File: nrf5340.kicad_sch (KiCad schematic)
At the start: 6 parts, among them U1 NRF5340

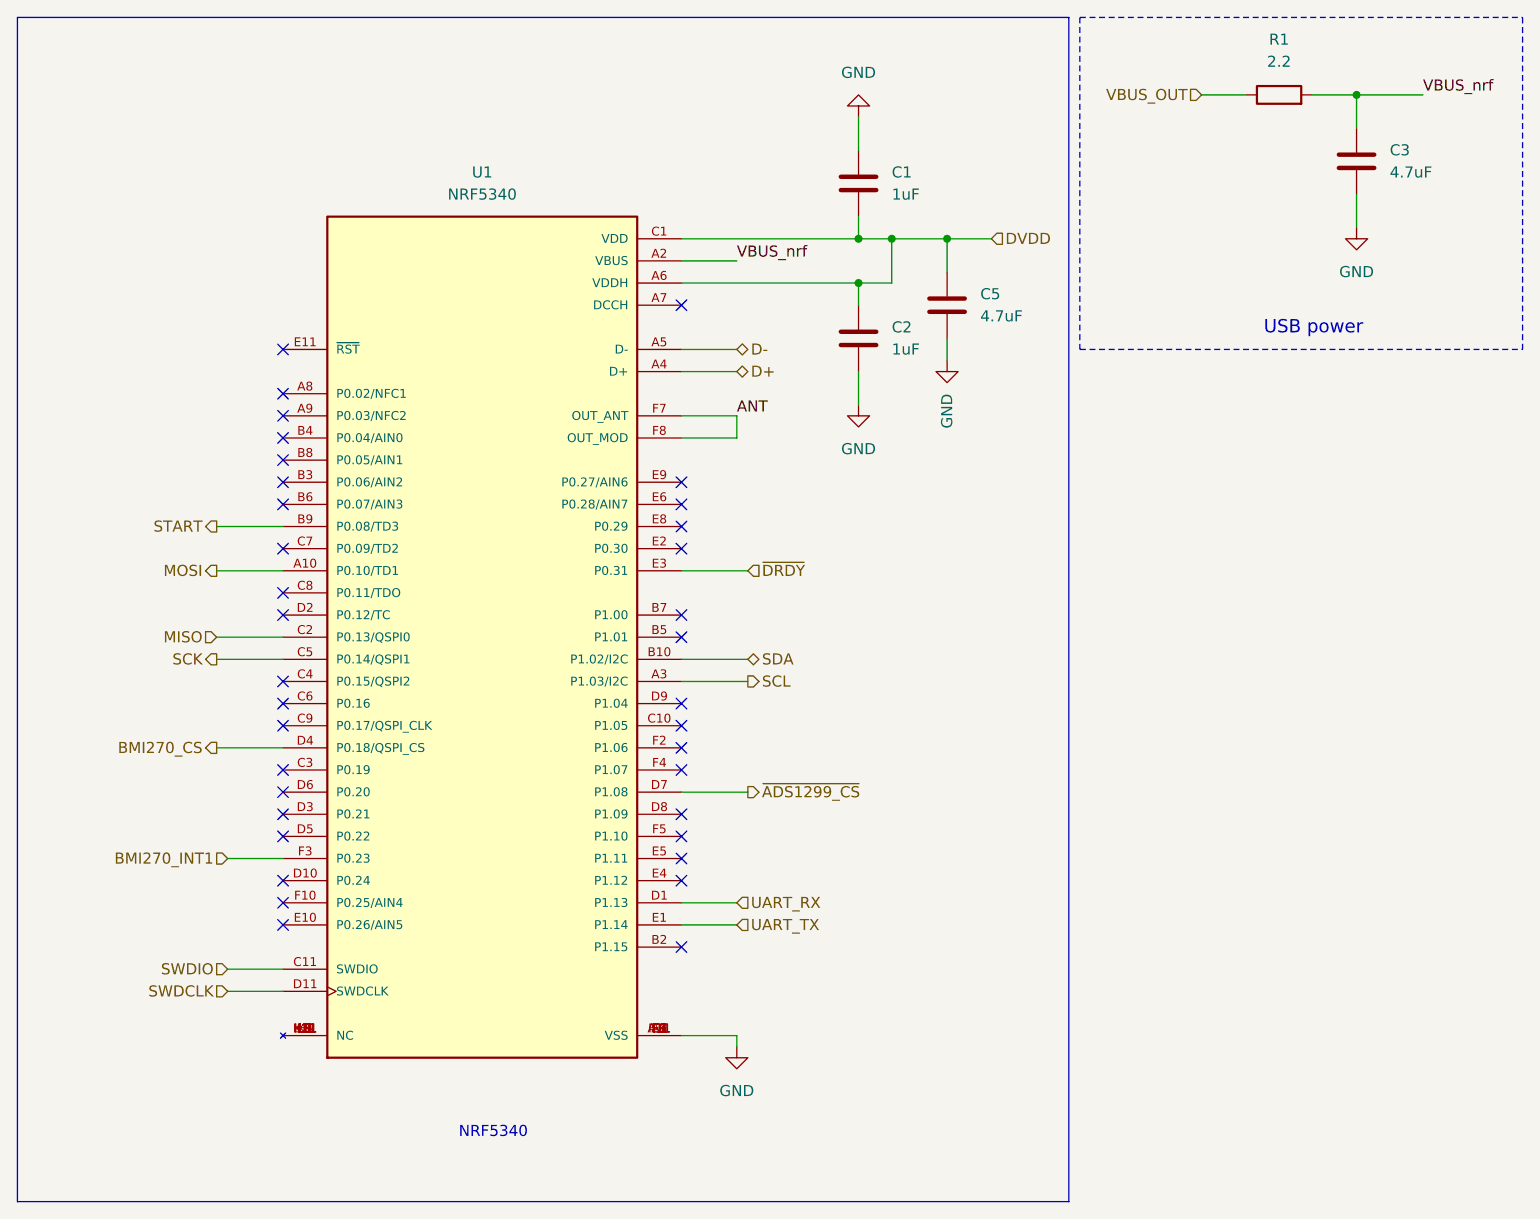
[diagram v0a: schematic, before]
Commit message: Feat: 개발보드 버전으로 PCB 변경
수정사항

단가 감소
- PCB Board size up (50x50)
- blind via 제거 (전체 레이아웃 수정)
- AVDD 전력평면 추가
- ADS1299 안쓰는핀 GND
- ADS1299 배치 변경 (Layout Reference 적용)

개발보드만 적용사항
- Pin Header size up 1.27 → 2.54mm
- PCB Size 50x50(mm)
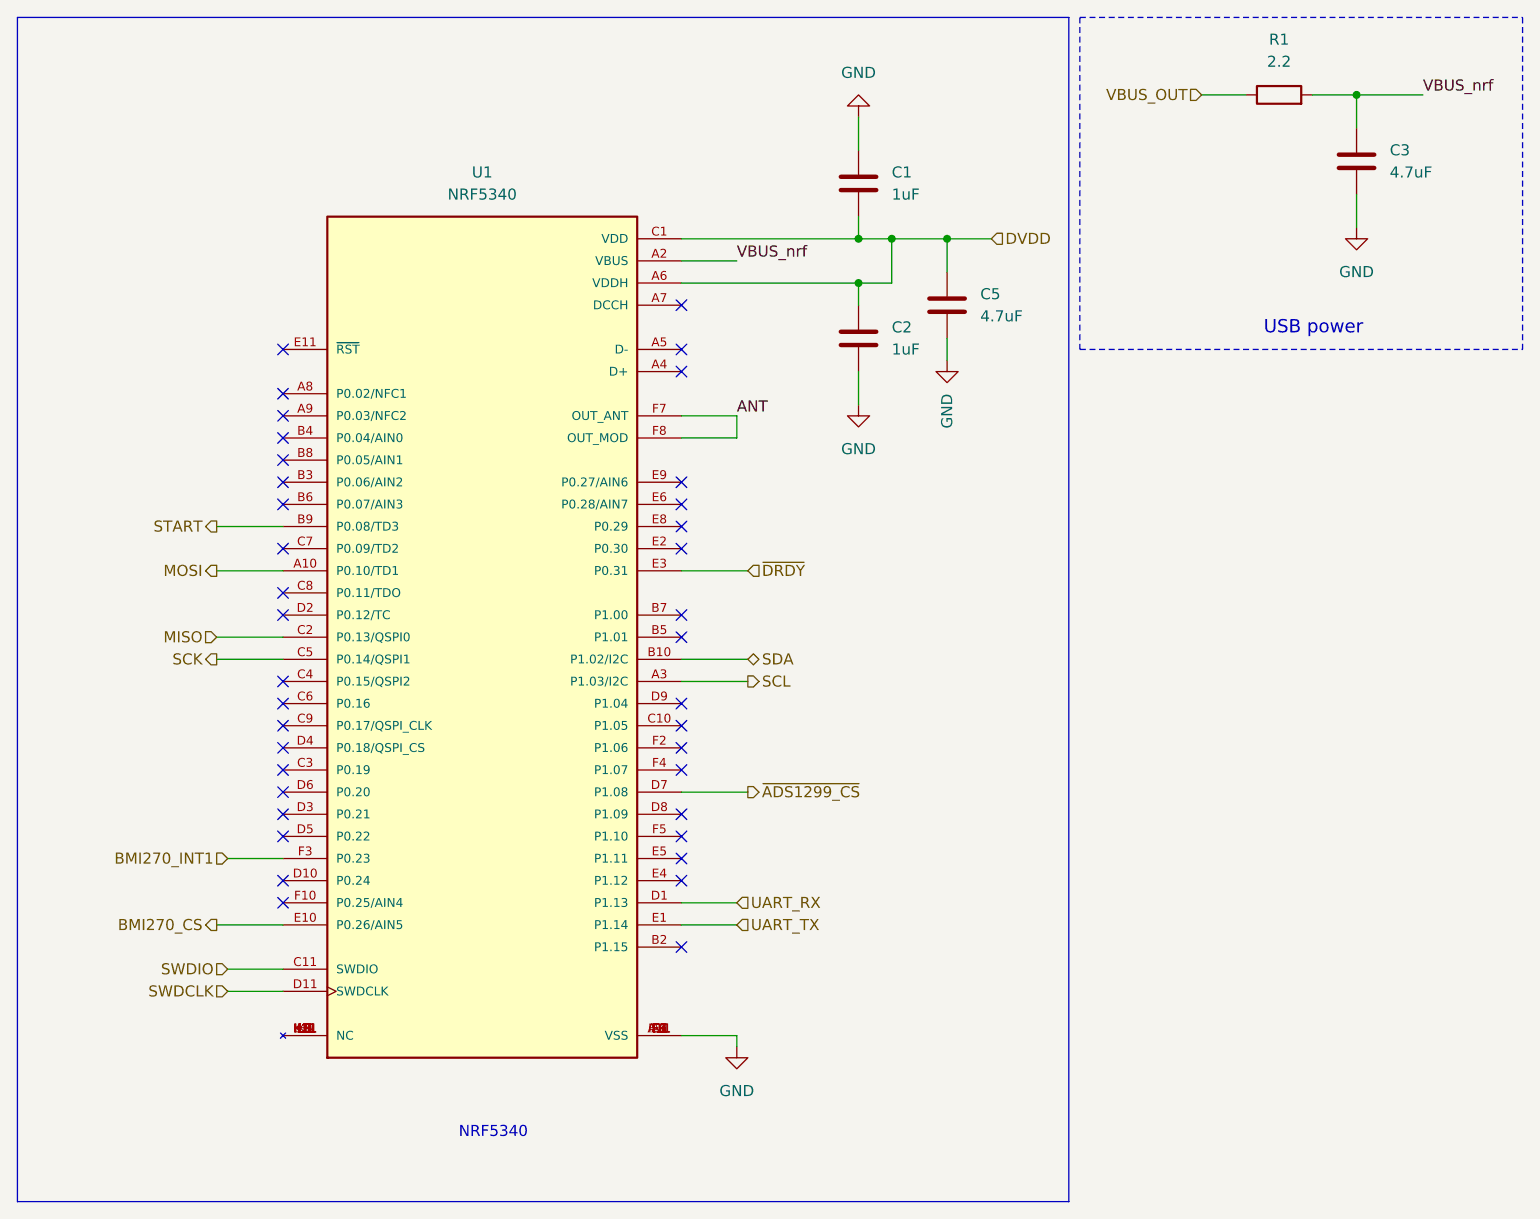
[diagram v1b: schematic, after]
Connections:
- net BMI270_CS: now also U1.E10 (P0.26/AIN5); no longer U1.D4 (P0.18/QSPI_CS)
- net D+: no longer names the net of U1.A4 (D+)
- net D-: no longer names the net of U1.A5 (D-)
- no-connect marks 36 -> 38
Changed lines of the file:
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@@
+	)
+	(no_connect
+		(at 43.18 66.04)
+	)
+	(no_connect
+		(at 43.18 73.66)
+	)
+	(no_connect
+		(at 88.9 66.04)
+	)
+	(no_connect
+		(at 43.18 55.88)
+	)
+	(no_connect
+		(at 88.9 45.72)
+	)
+	(no_connect
+		(at 88.9 83.82)
+	)
+	(no_connect
+		(at 88.9 81.28)
+	)
+	(no_connect
+		(at 88.9 68.58)
+	)
+	(no_connect
+		(at 88.9 111.76)
+	)
+	(no_connect
+		(at 43.18 104.14)
+	)
+	(no_connect
+		(at 88.9 53.34)
+	)
+	(no_connect
+		(at 43.18 91.44)
+	)
+	(no_connect
+		(at 88.9 119.38)
+	)
+	(no_connect
+		(at 43.18 78.74)
+	)
+	(no_connect
+		(at 43.18 68.58)
+	)
+	(no_connect
+		(at 88.9 109.22)
+	)
+	(no_connect
+		(at 43.18 93.98)
+	)
+	(no_connect
+		(at 43.18 63.5)
+	)
+	(no_connect
+		(at 88.9 91.44)
+	)
+	(no_connect
+		(at 88.9 73.66)
+	)
+	(no_connect
+		(at 88.9 104.14)
+	)
+	(no_connect
+		(at 88.9 99.06)
+	)
+	(no_connect
+		(at 88.9 50.8)
+	)
+	(no_connect
+		(at 43.18 99.06)
+	)
+	(no_connect
+		(at 43.18 111.76)
+	)
+	(no_connect
+		(at 43.18 101.6)
+	)
+	(no_connect
+		(at 43.18 60.96)
+	)
+	(no_connect
+		(at 43.18 58.42)
+	)
+	(no_connect
+		(at 88.9 96.52)
 	)
 	(no_connect
@@
 	)
 	(no_connect
-		(at 43.18 66.04)
-	)
-	(no_connect
-		(at 43.18 73.66)
-	)
-	(no_connect
-		(at 88.9 66.04)
-	)
-	(no_connect
-		(at 43.18 55.88)
-	)
-	(no_connect
-		(at 88.9 45.72)
-	)
-	(no_connect
-		(at 88.9 83.82)
-	)
-	(no_connect
-		(at 88.9 81.28)
-	)
-	(no_connect
-		(at 88.9 68.58)
-	)
-	(no_connect
-		(at 88.9 111.76)
-	)
-	(no_connect
-		(at 43.18 104.14)
-	)
-	(no_connect
-		(at 43.18 91.44)
-	)
-	(no_connect
-		(at 88.9 73.66)
-	)
-	(no_connect
-		(at 88.9 119.38)
-	)
-	(no_connect
-		(at 43.18 78.74)
-	)
-	(no_connect
-		(at 43.18 68.58)
-	)
-	(no_connect
-		(at 88.9 109.22)
-	)
-	(no_connect
-		(at 43.18 93.98)
-	)
-	(no_connect
-		(at 43.18 63.5)
-	)
-	(no_connect
-		(at 88.9 91.44)
+		(at 43.18 114.3)
+	)
+	(no_connect
+		(at 88.9 71.12)
+	)
+	(no_connect
+		(at 43.18 50.8)
+	)
+	(no_connect
+		(at 43.18 81.28)
 	)
 	(no_connect
@@
 	)
 	(no_connect
-		(at 88.9 104.14)
-	)
-	(no_connect
-		(at 88.9 99.06)
-	)
-	(no_connect
-		(at 43.18 114.3)
-	)
-	(no_connect
-		(at 43.18 99.06)
-	)
-	(no_connect
-		(at 43.18 111.76)
-	)
-	(no_connect
-		(at 43.18 60.96)
-	)
-	(no_connect
-		(at 43.18 58.42)
-	)
-	(no_connect
-		(at 88.9 71.12)
-	)
-	(no_connect
-		(at 43.18 101.6)
-	)
-	(no_connect
-		(at 43.18 50.8)
-	)
-	(no_connect
-		(at 43.18 81.28)
-	)
-	(no_connect
-		(at 43.18 116.84)
+		(at 43.18 96.52)
 	)
 	(no_connect
 		(at 88.9 93.98)
 	)
-	(no_connect
-		(at 88.9 96.52)
-	)
 	(wire
 		(pts
@@
 	(wire
 		(pts
+			(xy 35.56 116.84) (xy 43.18 116.84)
+		)
+		(stroke
+			(width 0)
+			(type default)
+		)
+	)
+	(wire
+		(pts
 			(xy 113.03 38.1) (xy 113.03 43.18)
 		)
@@
 	(wire
 		(pts
-			(xy 35.56 96.52) (xy 43.18 96.52)
-		)
-		(stroke
-			(width 0)
-			(type default)
-		)
-	)
-	(wire
-		(pts
 			(xy 95.25 130.81) (xy 95.25 129.54)
 		)
@@
 		)
 	)
-	(wire
-		(pts
-			(xy 88.9 53.34) (xy 95.25 53.34)
-		)
-		(stroke
-			(width 0)
-			(type default)
-		)
-	)
 	(polyline
 		(pts
@@
 		(pts
 			(xy 113.03 38.1) (xy 119.38 38.1)
-		)
-		(stroke
-			(width 0)
-			(type default)
-		)
-	)
-	(wire
-		(pts
-			(xy 88.9 50.8) (xy 95.25 50.8)
 		)
 		(stroke
@@
 		)
 	)
-	(hierarchical_label "D-"
-		(shape bidirectional)
-		(at 95.25 50.8 0)
+	(hierarchical_label "~{DRDY}"
+		(shape input)
+		(at 96.52 76.2 0)
 		(fields_autoplaced yes)
 		(effects
@@
 		)
 	)
-	(hierarchical_label "~{DRDY}"
-		(shape input)
-		(at 96.52 76.2 0)
-		(fields_autoplaced yes)
-		(effects
-			(font
-				(size 1.27 1.27)
-			)
-			(justify left)
+	(hierarchical_label "BMI270_CS"
+		(shape output)
+		(at 35.56 116.84 180)
+		(fields_autoplaced yes)
+		(effects
+			(font
+				(size 1.27 1.27)
+			)
+			(justify right)
 		)
 	)
@@
 		)
 	)
-	(hierarchical_label "D+"
-		(shape bidirectional)
-		(at 95.25 53.34 0)
-		(fields_autoplaced yes)
-		(effects
-			(font
-				(size 1.27 1.27)
-			)
-			(justify left)
-		)
-	)
 	(hierarchical_label "VBUS_OUT"
 		(shape input)
@@
 		(fields_autoplaced yes)
 		(effects
-			(font
-				(size 1.27 1.27)
-			)
-			(justify right)
-		)
-	)
-	(hierarchical_label "BMI270_CS"
-		(shape output)
-		(at 35.56 96.52 180)
-		(fields_autoplaced yes)
-		(effects
